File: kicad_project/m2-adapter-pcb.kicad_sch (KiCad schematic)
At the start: 0 parts

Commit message: Finish schematics
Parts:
- added C1, C2, C6, C7: 10uF, Capacitor_SMD:C_0805_2012Metric_Pad1.18x1.45mm_HandSolder, symbol Device:C
- added C3, C8, C9: 0.1uF, Capacitor_SMD:C_0805_2012Metric_Pad1.18x1.45mm_HandSolder, symbol Device:C
- added C4, C5: 22uF, Capacitor_SMD:C_0805_2012Metric_Pad1.18x1.45mm_HandSolder, symbol Device:C
- added D1: LED, LED_SMD:LED_0805_2012Metric_Pad1.15x1.40mm_HandSolder, symbol Device:LED
- added J1: Bus_M.2_Socket_B, m2-adapter-pcb:AMPHENOL_MDT420B03001, symbol m2-adapter-pcb:Bus_M.2_Socket_B_mod
- added J2: SATA-7P, m2-adapter-pcb:CONN_67490-1220_MOL, symbol m2-adapter-pcb:SATA-7P
- added J3: JST S2B-PH-K-S, Connector_JST:JST_PH_S2B-PH-K_1x02_P2.00mm_Horizontal, symbol Connector_Generic:Conn_01x02
- added L1: 3.3uH, Inductor_SMD:L_Vishay_IHLP-2525, symbol Device:L
- added R1, R3: 10kOhm, Resistor_SMD:R_0805_2012Metric_Pad1.20x1.40mm_HandSolder, symbol Device:R
- added R2: 220Ohm, Resistor_SMD:R_0805_2012Metric_Pad1.20x1.40mm_HandSolder, symbol Device:R
- added R4: 34kOhm, Resistor_SMD:R_0805_2012Metric_Pad1.20x1.40mm_HandSolder, symbol Device:R
- added U1: TPS563200, Package_TO_SOT_SMD:SOT-23-6, symbol Regulator_Switching:TPS563200
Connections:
- new net: R3.1, R4.1, U1.4 (VFB)
- new net: C1.1, C2.1, J3.2 (Pin_2), U1.3 (VIN), U1.5 (EN)
- new net: J1.49 (PETp0/SATA-A+), J2.2 (A+)
- new net: J1.47 (PETn0/SATA-A-), J2.3 (A-)
- new net: J1.43 (PERp0/SATA-B-), J2.5 (B-)
- new net: J1.41 (PERn0/SATA-B+), J2.6 (B+)
- new net: D1.1 (K), J1.10 (GPIO_9/DAS/~{DSS}/~{LED1})
- new net: D1.2 (A), R2.2
- new net: C3.1, L1.1, U1.2 (SW)
- new net: C3.2, U1.6 (VBST)
- new net: J1.38 (DEVSLP), R1.1
- new net +3.3V: C4.1, C5.1, C6.1, C7.1, C8.1, C9.1, J1.2 (3.3V), J1.4 (3.3V), J1.70 (3.3V), J1.72 (3.3V), J1.74 (3.3V), L1.2, R2.1, R4.2
- new net GND: C1.2, C2.2, C4.2, C5.2, C6.2, C7.2, C8.2, C9.2, J1.11 (GND), J1.27 (GND), J1.3 (GND), J1.33 (GND), J1.39 (GND), J1.45 (GND), J1.5 (GND), J1.51 (GND), J1.57 (GND), J1.71 (GND), J1.73 (GND), J1.P1 (GND), J1.P2 (GND), J2.1 (GND), J2.4 (GND), J2.7 (GND), J2.8 (SHIELD), J3.1 (Pin_1), R1.2, R3.2, U1.1 (GND)
- no-connect marks 0 -> 43
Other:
- note added: "20mOhm"
- note added: "3mOhm"
- note added: "Drive activity LED"
- note added: "M.2 to SATA SSD adapter PCB"
- note added: "Power input"
- note added: "SATA connector"

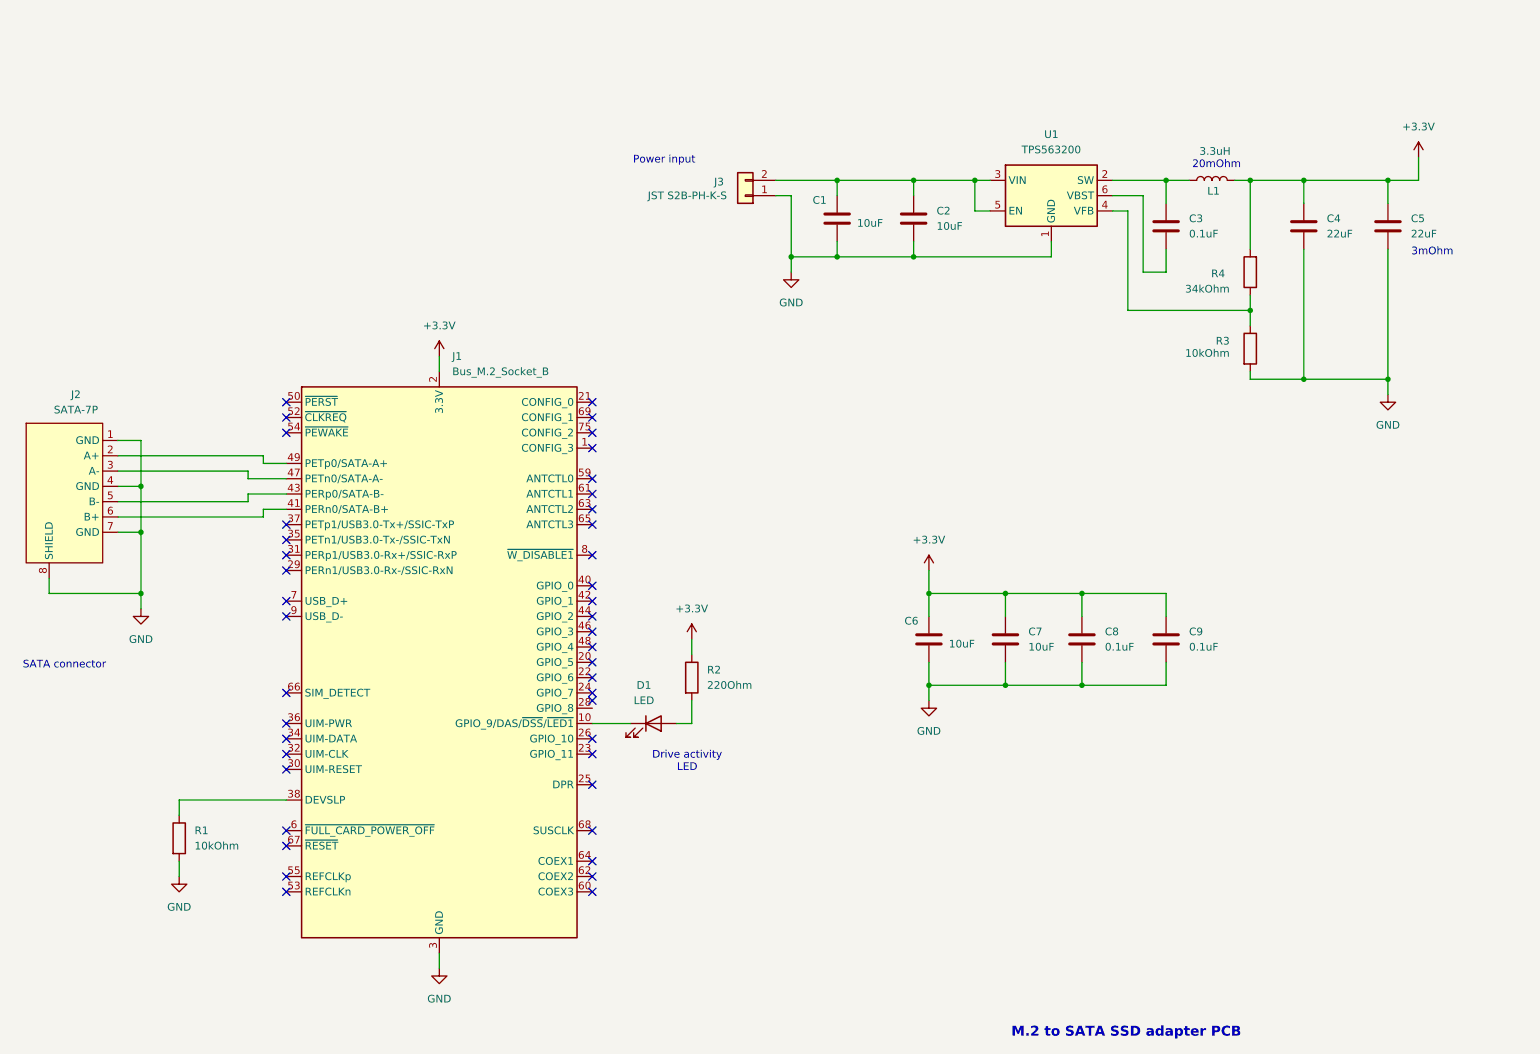
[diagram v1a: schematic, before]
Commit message: Update buck converter schematics
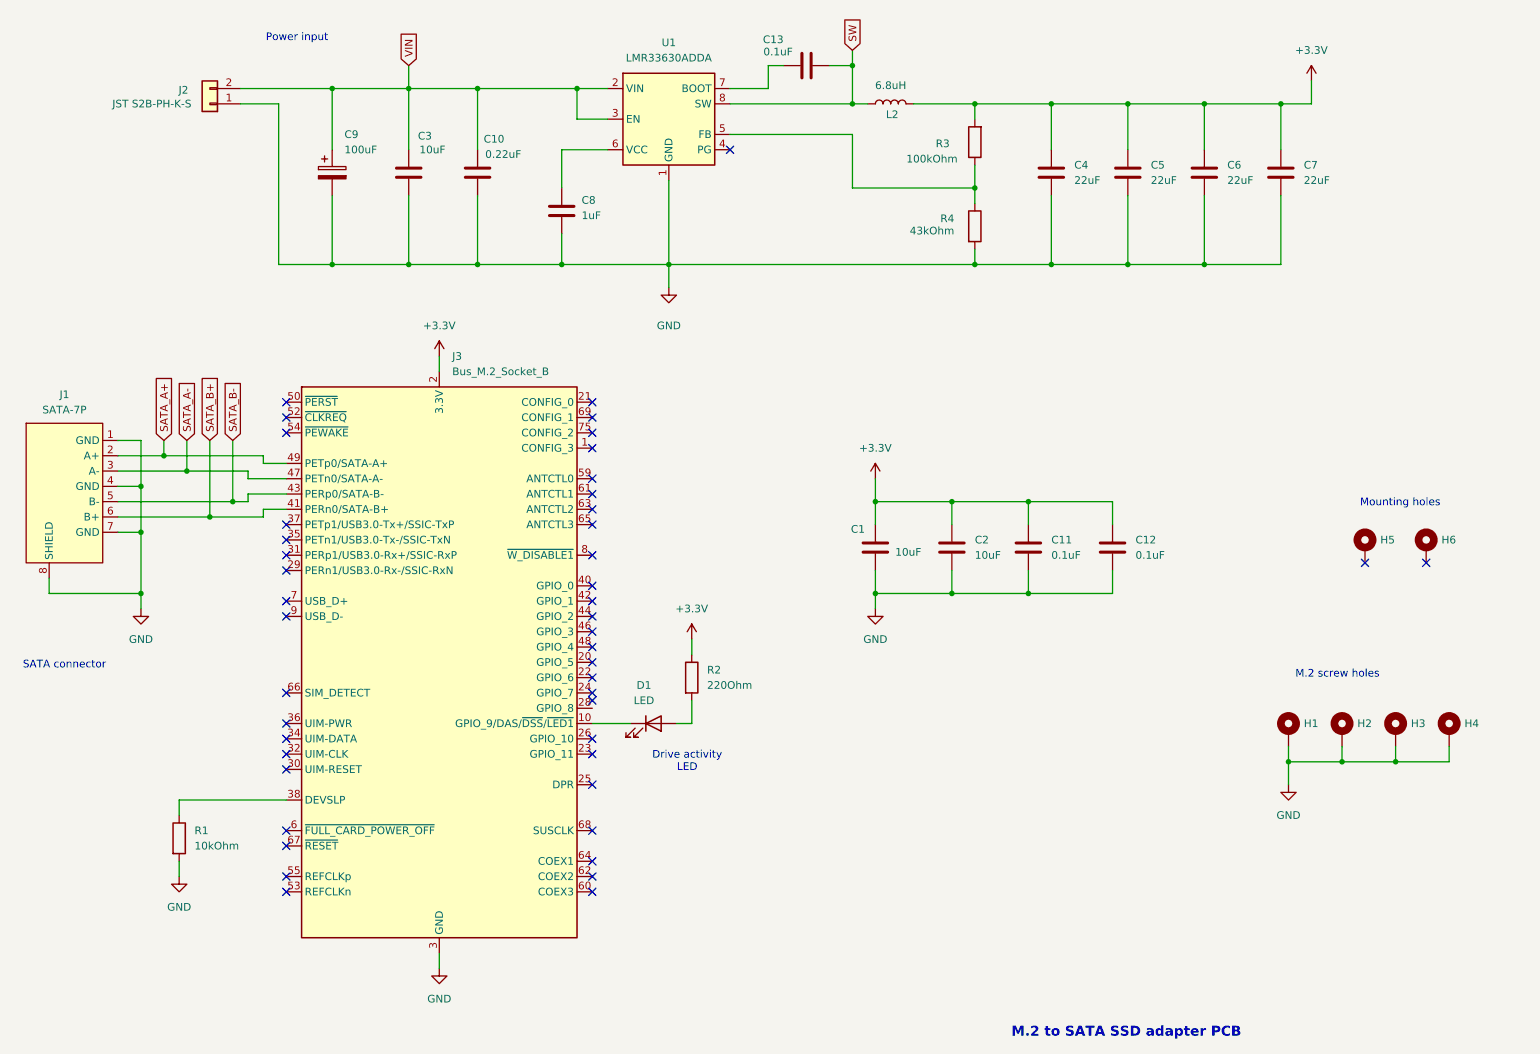
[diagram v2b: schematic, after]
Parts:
- removed C1, C2: 10uF, Capacitor_SMD:C_0805_2012Metric_Pad1.18x1.45mm_HandSolder, symbol Device:C
- removed J3: JST S2B-PH-K-S, Connector_JST:JST_PH_S2B-PH-K_1x02_P2.00mm_Horizontal, symbol Connector_Generic:Conn_01x02
- removed L1: 3.3uH, Inductor_SMD:L_Vishay_IHLP-2525, symbol Device:L
- removed U1: TPS563200, Package_TO_SOT_SMD:SOT-23-6, symbol Regulator_Switching:TPS563200
- added C10: 0.22uF, Capacitor_SMD:C_0805_2012Metric_Pad1.18x1.45mm_HandSolder, symbol Device:C
- added C13: 0.1uF, Capacitor_SMD:C_0805_2012Metric_Pad1.18x1.45mm_HandSolder, symbol Device:C
- added C6, C7: 22uF, Capacitor_SMD:C_1210_3225Metric_Pad1.33x2.70mm_HandSolder, symbol Device:C
- added C8: 1uF, Capacitor_SMD:C_0805_2012Metric_Pad1.18x1.45mm_HandSolder, symbol Device:C
- added C9: 100uF, Capacitor_SMD:C_Elec_8x6.2, symbol Device:C_Polarized
- added H1, H2, H3, H4: MountingHole_Pad, m2-adapter-pcb:M.2_Standoff_Hole, symbol Mechanical:MountingHole_Pad
- added H5, H6: MountingHole_Pad, MountingHole:MountingHole_2.2mm_M2_Pad, symbol Mechanical:MountingHole_Pad
- added J2: JST S2B-PH-K-S, Connector_JST:JST_PH_S2B-PH-K_1x02_P2.00mm_Horizontal, symbol Connector_Generic:Conn_01x02
- added L2: 6.8uH, m2-adapter-pcb:L_MPX1D0840, symbol Device:L
- added U1: LMR33630ADDA, Package_SO:Texas_HSOP-8-1EP_3.9x4.9mm_P1.27mm_ThermalVias, symbol Regulator_Switching:LMR33630ADDA
- C1: renamed from C6; footprint Capacitor_SMD:C_0805_2012Metric_Pad1.18x1.45mm_HandSolder -> Capacitor_SMD:C_1206_3216Metric_Pad1.33x1.80mm_HandSolder; Link (none) -> https://www.tme.eu/it/en/details/cl31b106kbhnnne/mlcc-smd-c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
- C11: renamed from C8; Link (none) -> https://www.tme.eu/it/en/details/0805b104k500ct/mlcc-smd-ca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
- C12: renamed from C9; Link (none) -> https://www.tme.eu/it/en/details/0805b104k500ct/mlcc-smd-ca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
- C2: renamed from C7; footprint Capacitor_SMD:C_0805_2012Metric_Pad1.18x1.45mm_HandSolder -> Capacitor_SMD:C_1206_3216Metric_Pad1.33x1.80mm_HandSolder; Link (none) -> https://www.tme.eu/it/en/details/cl31b106kbhnnne/mlcc-smd-c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
- C3: value 0.1uF -> 10uF; footprint Capacitor_SMD:C_0805_2012Metric_Pad1.18x1.45mm_HandSolder -> Capacitor_SMD:C_1206_3216Metric_Pad1.33x1.80mm_HandSolder; Link (none) -> https://www.tme.eu/it/en/details/cl31b106kbhnnne/mlcc-smd-c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
- C4, C5: footprint Capacitor_SMD:C_0805_2012Metric_Pad1.18x1.45mm_HandSolder -> Capacitor_SMD:C_1210_3225Metric_Pad1.33x2.70mm_HandSolder; Link (none) -> https://www.tme.eu/it/en/details/cl32b226kajnnne/mlcc-smd-c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
- R1: Link (none) -> https://www.tme.eu/it/en/details/ac0805fr-0710kl/smd-resist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
- R2: Link (none) -> https://www.tme.eu/it/en/details/rca0805220rjnea/smd-resist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
- R3: value 10kOhm -> 100kOhm; Link (none) -> https://www.tme.eu/it/en/details/rc0805fr-07100k/smd-resist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
- R4: value 34kOhm -> 43kOhm; Link (none) -> https://www.tme.eu/it/en/details/era6aeb433v/smd-resistors/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
- renumbered J2 to J1, J1 to J3
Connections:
- net +3.3V: now also R3.2, C6.1, C7.1, L2.2; no longer R4.2
- net GND: now also C3.2, R4.2, C10.2, C6.2, C7.2, C8.2, C9.2, H1.1, H2.1, H3.1, H4.1, J2.1 (Pin_1), U1.1 (GND), U1.9 (GND); no longer R3.2
- net at R3.1, R4.1: now also U1.5 (FB)
- net SATA_A+: now reaches J1.2 (A+), J3.49 (PETp0/SATA-A+)
- net SATA_A-: now reaches J1.3 (A-), J3.47 (PETn0/SATA-A-)
- net SATA_B-: now reaches J1.5 (B-), J3.43 (PERp0/SATA-B-)
- net SATA_B+: now reaches J1.6 (B+), J3.41 (PERn0/SATA-B+)
- net VIN: now reaches C3.1
- net VIN: now also C10.1, C9.1, J2.2 (Pin_2), U1.2 (VIN), U1.3 (EN)
- new net: C13.1, U1.7 (BOOT)
- new net: C8.1, U1.6 (VCC)
- new net SW: C13.2, L2.1, U1.8 (SW)
- no-connect marks 43 -> 46
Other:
- note added: "M.2 screw holes"
- note added: "Mounting holes"
- note removed: "20mOhm"
- note removed: "3mOhm"
- moved on the sheet: C1, C11, C12, C2

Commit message: Finish routing
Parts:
- J1: footprint m2-adapter-pcb:CONN_67490-1220_MOL -> m2-adapter-pcb:AMPHENOL_SAT3M2132072TR
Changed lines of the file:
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@@
 	)
 	(no_connect
-		(at 116.84 134.62)
+		(at 116.84 135.89)
 	)
 	(no_connect
@@
 			)
 		)
-		(property "Footprint" "m2-adapter-pcb:CONN_67490-1220_MOL"
+		(property "Footprint" "m2-adapter-pcb:AMPHENOL_SAT3M2132072TR"
 			(at 30.48 97.79 0)
 			(effects

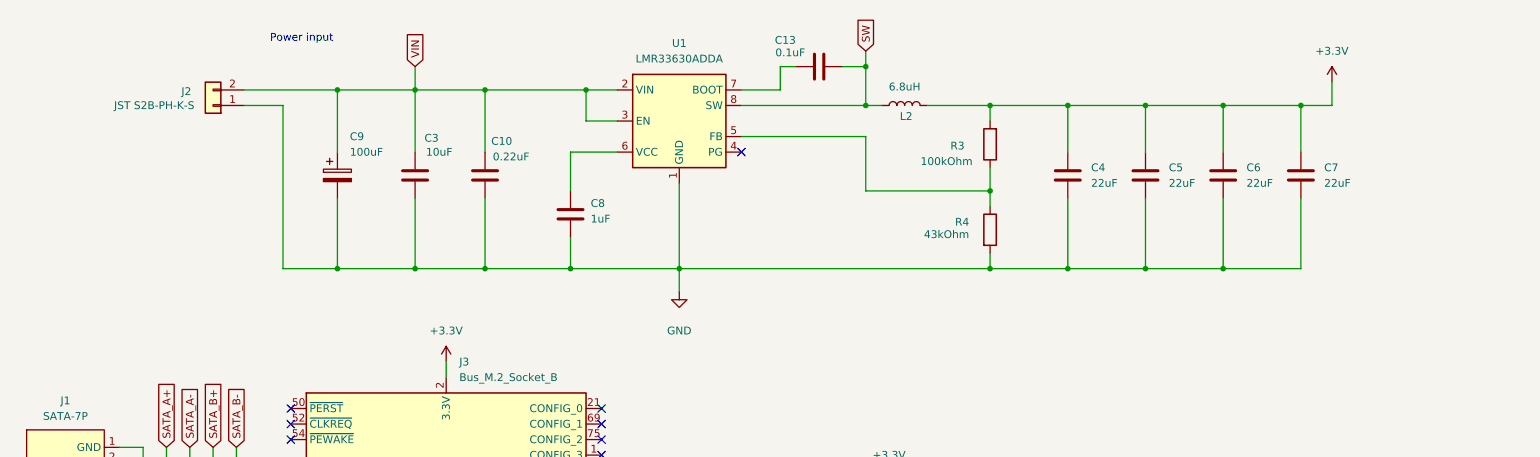
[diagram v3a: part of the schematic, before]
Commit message: Buck converter redesign
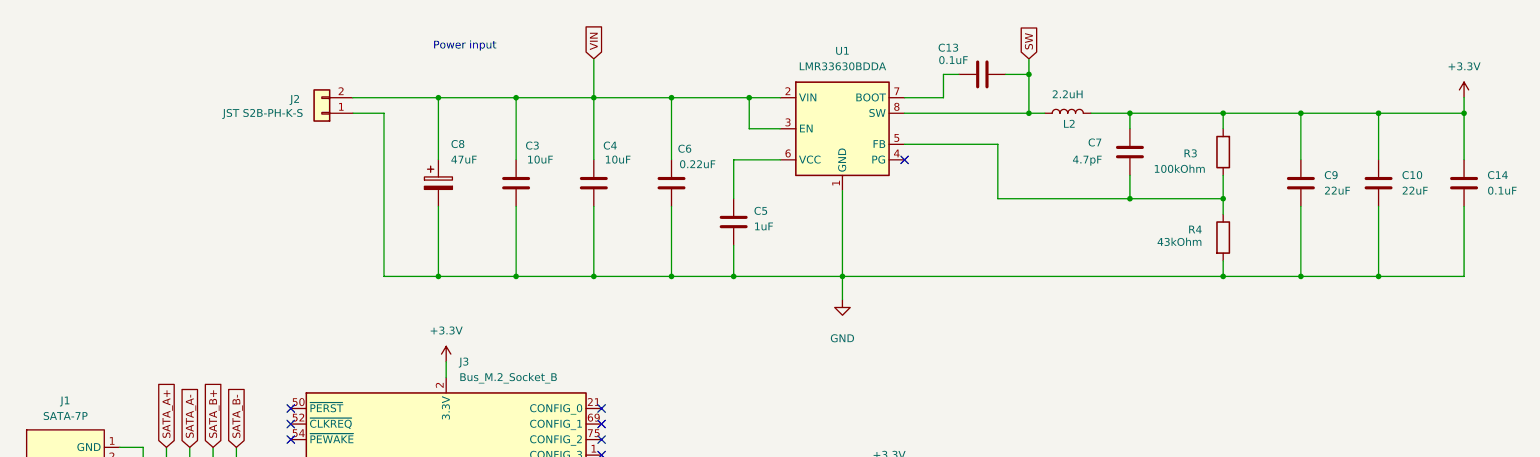
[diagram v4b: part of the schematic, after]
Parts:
- removed C6: 22uF, Capacitor_SMD:C_1210_3225Metric_Pad1.33x2.70mm_HandSolder, symbol Device:C
- added C14: 0.1uF, Capacitor_SMD:C_0805_2012Metric_Pad1.18x1.45mm_HandSolder, symbol Device:C
- added C4: 10uF, Capacitor_SMD:C_1206_3216Metric_Pad1.33x1.80mm_HandSolder, symbol Device:C
- C1, C2, C3: Link https://www.tme.eu/it/en/details/cl31b106kbhnnne/mlcc-smd-c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 -> https://www.digikey.it/it/products/detail/samsung-electro-m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
- C10: renamed from C5; Link https://www.tme.eu/it/en/details/cl32b226kajnnne/mlcc-smd-c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 -> https://www.digikey.it/it/products/detail/samsung-electro-m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
- C11, C12, C13: Link https://www.tme.eu/it/en/details/0805b104k500ct/mlcc-smd-ca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 -> https://www.digikey.it/it/products/detail/samsung-electro-m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
- C5: renamed from C8; Link https://www.tme.eu/it/en/details/cl21b105kbfnnne/mlcc-smd-c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 -> (none)
- C6: renamed from C10; Link https://www.tme.eu/it/en/details/cl21b224kbfnnng/mlcc-smd-c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 -> https://www.digikey.it/it/products/detail/samsung-electro-m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
- C7: value 22uF -> 4.7pF; footprint Capacitor_SMD:C_1210_3225Metric_Pad1.33x2.70mm_HandSolder -> Capacitor_SMD:C_0805_2012Metric_Pad1.18x1.45mm_HandSolder; Link https://www.tme.eu/it/en/details/cl32b226kajnnne/mlcc-smd-c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 -> (none)
- C8: renamed from C9; value 100uF -> 47uF; footprint Capacitor_SMD:C_Elec_8x6.2 -> Capacitor_SMD:C_Elec_6.3x5.8; Link https://www.tme.eu/it/en/details/ucl1e101mcl6gs/smd-electro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 -> https://www.digikey.it/it/products/detail/kemet/A768EB476M1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
- C9: renamed from C4; Link https://www.tme.eu/it/en/details/cl32b226kajnnne/mlcc-smd-c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 -> https://www.digikey.it/it/products/detail/samsung-electro-m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
- J1: Link (none) -> https://www.digikey.it/it/products/detail/amphenol-cs-fci/S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
- J3: Link (none) -> https://www.digikey.it/it/products/detail/amphenol-cs-fci/M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
- L2: value 6.8uH -> 2.2uH; footprint m2-adapter-pcb:L_MPX1D0840 -> m2-adapter-pcb:L_AMDLA4530S; Link https://www.tme.eu/it/en/details/mpx1d0840l6r8/inductors/ke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 -> https://www.digikey.it/it/products/detail/abracon-llc/AMDLA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
- R1: Link https://www.tme.eu/it/en/details/ac0805fr-0710kl/smd-resist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 -> (none)
- R2: Link https://www.tme.eu/it/en/details/rca0805220rjnea/smd-resist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 -> (none)
- R3: Link https://www.tme.eu/it/en/details/rc0805fr-07100k/smd-resist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 -> (none)
- R4: Link https://www.tme.eu/it/en/details/era6aeb433v/smd-resistors/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 -> (none)
- U1: value LMR33630ADDA -> LMR33630BDDA; footprint Package_SO:Texas_HSOP-8-1EP_3.9x4.9mm_P1.27mm_ThermalVias -> m2-adapter-pcb:Texas_HSOP-8-1EP_3.9x4.9mm_P1.27mm_ThermalVias_HandSolder; Link https://www.digikey.it/it/products/detail/texas-instruments/LMR33630ADDAR/8554847 -> https://www.digikey.it/it/products/detail/texas-instruments/LMR33630BDDA/8571550
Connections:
- net +3.3V: now also C14.1
- net GND: now also C14.2, C4.2; no longer C7.2
- net VIN: now also C4.1
- net at R3.1, R4.1, U1.5 (FB): now also C7.2
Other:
- moved on the sheet: C10, C13, C3, C5, C6, C8, C9, J2, L2, R3, R4, U1

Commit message: Add test points
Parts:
- added TP1, TP2: TestPoint, TestPoint:TestPoint_Pad_D2.0mm, symbol Connector:TestPoint
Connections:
- net +3.3V: now also TP2.1
- net GND: now also TP1.1
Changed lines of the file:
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@@
 	)
 	(junction
+		(at 81.28 63.5)
+		(diameter 0)
+		(color 0 0 0 0)
+	)
+	(junction
 		(at 128.27 34.29)
 		(diameter 0)
@@
 	(wire
 		(pts
+			(xy 265.43 36.83) (xy 257.81 36.83)
+		)
+		(stroke
+			(width 0)
+			(type default)
+		)
+	)
+	(wire
+		(pts
 			(xy 115.57 34.29) (xy 115.57 44.45)
 		)
@@
 	(wire
 		(pts
+			(xy 69.85 63.5) (xy 81.28 63.5)
+		)
+		(stroke
+			(width 0)
+			(type default)
+		)
+	)
+	(wire
+		(pts
 			(xy 176.53 101.6) (xy 163.83 101.6)
 		)
@@
 	(wire
 		(pts
+			(xy 265.43 35.56) (xy 265.43 36.83)
+		)
+		(stroke
+			(width 0)
+			(type default)
+		)
+	)
+	(wire
+		(pts
 			(xy 90.17 52.07) (xy 90.17 63.5)
 		)
@@
 	(wire
 		(pts
+			(xy 69.85 59.69) (xy 69.85 63.5)
+		)
+		(stroke
+			(width 0)
+			(type default)
+		)
+	)
+	(wire
+		(pts
 			(xy 250.19 142.24) (xy 250.19 144.78)
 		)
@@
 	)
 	(symbol
+		(lib_id "Connector:TestPoint")
+		(at 69.85 59.69 0)
+		(unit 1)
+		(exclude_from_sim no)
+		(in_bom yes)
+		(on_board yes)
+		(dnp no)
+		(fields_autoplaced yes)
+		(property "Reference" "TP1"
+			(at 72.39 56.3879 0)
+			(effects
+				(font
+					(size 1.27 1.27)
+				)
+				(justify left)
+			)
+		)
+		(property "Value" "TestPoint"
+			(at 72.39 57.6579 0)
+			(effects
+				(font
+					(size 1.27 1.27)
+				)
+				(justify left)
+				(hide yes)
+			)
+		)
+		(property "Footprint" "TestPoint:TestPoint_Pad_D2.0mm"
+			(at 74.93 59.69 0)
+			(effects
+				(font
+					(size 1.27 1.27)
+				)
+				(hide yes)
+			)
+		)
+		(property "Datasheet" "~"
+			(at 74.93 59.69 0)
+			(effects
+				(font
+					(size 1.27 1.27)
+				)
+				(hide yes)
+			)
+		)
+		(property "Description" "test point"
+			(at 69.85 59.69 0)
+			(effects
+				(font
+					(size 1.27 1.27)
+				)
+				(hide yes)
+			)
+		)
+		(pin "1"
+		)
+		(instances
+			(project "m2-adapter-pcb"
+				(path "/67cc31b6-bc6f-4820-88e4-a7b744a09688"
+					(reference "TP1")
+					(unit 1)
+				)
+			)
+		)
+	)
+	(symbol
 		(lib_id "power:GND")
 		(at 48.26 163.83 0)
@@
 					(unit 1)
 				)
+			)
+		)
+	)
+	(symbol
+		(lib_id "Connector:TestPoint")
+		(at 265.43 35.56 0)
+		(unit 1)
+		(exclude_from_sim no)
+		(in_bom yes)
+		(on_board yes)
+		(dnp no)
+		(fields_autoplaced yes)
+		(property "Reference" "TP2"
+			(at 267.97 32.2579 0)
+			(effects
+				(font
+					(size 1.27 1.27)
+				)
+				(justify left)
+			)
+		)
+		(property "Value" "TestPoint"
+			(at 267.97 33.5279 0)
+			(effects
+				(font
+					(size 1.27 1.27)
+				)
+				(justify left)
+				(hide yes)
+			)
+		)
+		(property "Footprint" "TestPoint:TestPoint_Pad_D2.0mm"
+			(at 270.51 35.56 0)
+			(effects
+				(font
+					(size 1.27 1.27)
+				)
+				(hide yes)
+			)
+		)
+		(property "Datasheet" "~"
+			(at 270.51 35.56 0)
+			(effects
+				(font
+					(size 1.27 1.27)
+				)
+				(hide yes)
+			)
+		)
+		(property "Description" "test point"
+			(at 265.43 35.56 0)
+			(effects
+				(font
+					(size 1.27 1.27)
+				)
+				(hide yes)
+			)
+		)
+		(pin "1"
+		)
+		(instances
+			(project ""
+				(path "/67cc31b6-bc6f-4820-88e4-a7b744a09688"
+					(reference "TP2")
+					(unit 1)
+				)
